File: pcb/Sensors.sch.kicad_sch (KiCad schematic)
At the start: 22 parts, among them J1 53398-0371, J2 53398-0371, J3 Conn_01x04_Pin, J4 53398-0371, J5 53398-0371, J6 53398-0371, J7 53398-0371, J8 53398-0371, J9 53398-0371, U2 BMP280

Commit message: Drobne poprawki w schemacie elektrycznym
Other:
- moved on the sheet: J3
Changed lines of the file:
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@@
 	(wire
 		(pts
-			(xy 198.12 72.39) (xy 198.12 69.85)
+			(xy 121.92 85.09) (xy 121.92 100.33)
 		)
 		(stroke
@@
 	(wire
 		(pts
-			(xy 121.92 85.09) (xy 121.92 100.33)
+			(xy 106.68 116.84) (xy 106.68 118.11)
 		)
 		(stroke
@@
 	(wire
 		(pts
-			(xy 106.68 116.84) (xy 106.68 118.11)
+			(xy 86.36 171.45) (xy 91.44 171.45)
 		)
 		(stroke
@@
 	(wire
 		(pts
-			(xy 86.36 171.45) (xy 91.44 171.45)
+			(xy 86.36 173.99) (xy 91.44 173.99)
 		)
 		(stroke
@@
 	(wire
 		(pts
-			(xy 86.36 173.99) (xy 91.44 173.99)
+			(xy 167.64 124.46) (xy 167.64 125.73)
 		)
 		(stroke
@@
 	(wire
 		(pts
-			(xy 167.64 124.46) (xy 167.64 125.73)
+			(xy 105.41 45.72) (xy 102.87 45.72)
 		)
 		(stroke
@@
 	(wire
 		(pts
-			(xy 105.41 45.72) (xy 102.87 45.72)
+			(xy 109.22 116.84) (xy 121.92 116.84)
 		)
 		(stroke
@@
 	(wire
 		(pts
-			(xy 109.22 116.84) (xy 121.92 116.84)
+			(xy 176.53 58.42) (xy 176.53 62.23)
 		)
 		(stroke
@@
 	(wire
 		(pts
+			(xy 176.53 67.31) (xy 180.34 67.31)
+		)
+		(stroke
+			(width 0)
+			(type default)
+		)
+	)
+	(wire
+		(pts
 			(xy 104.14 118.11) (xy 104.14 116.84)
 		)
@@
 	(wire
 		(pts
-			(xy 185.42 81.28) (xy 189.23 81.28)
-		)
-		(stroke
-			(width 0)
-			(type default)
-		)
-	)
-	(wire
-		(pts
 			(xy 121.92 50.8) (xy 123.19 50.8)
 		)
@@
 	(wire
 		(pts
-			(xy 198.12 69.85) (xy 185.42 69.85)
-		)
-		(stroke
-			(width 0)
-			(type default)
-		)
-	)
-	(wire
-		(pts
 			(xy 76.2 102.87) (xy 77.47 102.87)
 		)
@@
 	(wire
 		(pts
-			(xy 185.42 72.39) (xy 185.42 81.28)
-		)
-		(stroke
-			(width 0)
-			(type default)
-		)
-	)
-	(wire
-		(pts
 			(xy 78.74 106.68) (xy 77.47 106.68)
 		)
@@
 	(wire
 		(pts
-			(xy 185.42 64.77) (xy 189.23 64.77)
-		)
-		(stroke
-			(width 0)
-			(type default)
-		)
-	)
-	(wire
-		(pts
 			(xy 104.14 184.15) (xy 104.14 186.69)
 		)
@@
 	(wire
 		(pts
-			(xy 185.42 67.31) (xy 189.23 67.31)
+			(xy 123.19 48.26) (xy 123.19 50.8)
 		)
 		(stroke
@@
 	(wire
 		(pts
-			(xy 123.19 48.26) (xy 123.19 50.8)
+			(xy 176.53 69.85) (xy 180.34 69.85)
 		)
 		(stroke
@@
 	(wire
 		(pts
+			(xy 176.53 64.77) (xy 199.39 64.77)
+		)
+		(stroke
+			(width 0)
+			(type default)
+		)
+	)
+	(wire
+		(pts
 			(xy 73.66 160.02) (xy 73.66 179.07)
 		)
@@
 	(hierarchical_label "MQ135_AOUT"
 		(shape output)
-		(at 189.23 67.31 0)
+		(at 180.34 67.31 0)
 		(fields_autoplaced yes)
 		(effects
@@
 	(hierarchical_label "MQ135_DOUT"
 		(shape output)
-		(at 189.23 64.77 0)
+		(at 180.34 69.85 0)
 		(fields_autoplaced yes)
 		(effects
@@
 	(symbol
 		(lib_id "power:+3.3V")
-		(at 189.23 81.28 0)
+		(at 176.53 58.42 0)
 		(unit 1)
 		(exclude_from_sim no)
@@
 		(dnp no)
 		(property "Reference" "#PWR021"
-			(at 189.23 85.09 0)
+			(at 176.53 62.23 0)
 			(effects
 				(font
@@
 		)
 		(property "Value" "+3.3V"
-			(at 189.23 77.47 0)
+			(at 176.53 54.61 0)
 			(effects
 				(font
@@
 		)
 		(property "Footprint" ""
-			(at 189.23 81.28 0)
+			(at 176.53 58.42 0)
 			(effects
 				(font
@@
 		)
 		(property "Datasheet" ""
-			(at 189.23 81.28 0)
+			(at 176.53 58.42 0)
 			(effects
 				(font
@@
 		)
 		(property "Description" "Power symbol creates a global label with name \"+3.3V\""
-			(at 189.23 81.28 0)
+			(at 176.53 58.42 0)
 			(effects
 				(font
@@
 	(symbol
 		(lib_id "Connector:Conn_01x04_Pin")
-		(at 180.34 67.31 0)
+		(at 171.45 67.31 0)
+		(mirror x)
 		(unit 1)
 		(exclude_from_sim no)
@@
 		(on_board yes)
 		(dnp no)
-		(fields_autoplaced yes)
 		(property "Reference" "J3"
-			(at 180.975 59.69 0)
+			(at 172.085 74.93 0)
 			(effects
 				(font
@@
 		)
 		(property "Value" "Conn_01x04_Pin"
-			(at 180.975 62.23 0)
+			(at 172.085 72.39 0)
 			(effects
 				(font
@@
 		)
 		(property "Footprint" "1bmoje:533980471- MOLEXx4"
-			(at 180.34 67.31 0)
+			(at 171.45 67.31 0)
 			(effects
 				(font
@@
 		)
 		(property "Datasheet" "~"
-			(at 180.34 67.31 0)
+			(at 171.45 67.31 0)
 			(effects
 				(font
@@
 		)
 		(property "Description" "Generic connector, single row, 01x04, script generated"
-			(at 180.34 67.31 0)
+			(at 171.45 67.31 0)
 			(effects
 				(font
@@
 	(symbol
 		(lib_id "power:GND")
-		(at 198.12 72.39 0)
+		(at 199.39 64.77 0)
 		(unit 1)
 		(exclude_from_sim no)
@@
 		(fields_autoplaced yes)
 		(property "Reference" "#PWR022"
-			(at 198.12 78.74 0)
+			(at 199.39 71.12 0)
 			(effects
 				(font
@@
 		)
 		(property "Value" "GND"
-			(at 198.12 77.47 0)
+			(at 199.39 69.85 0)
 			(effects
 				(font
@@
 		)
 		(property "Footprint" ""
-			(at 198.12 72.39 0)
+			(at 199.39 64.77 0)
 			(effects
 				(font
@@
 		)
 		(property "Datasheet" ""
-			(at 198.12 72.39 0)
+			(at 199.39 64.77 0)
 			(effects
 				(font
@@
 		)
 		(property "Description" "Power symbol creates a global label with name \"GND\" , ground"
-			(at 198.12 72.39 0)
+			(at 199.39 64.77 0)
 			(effects
 				(font

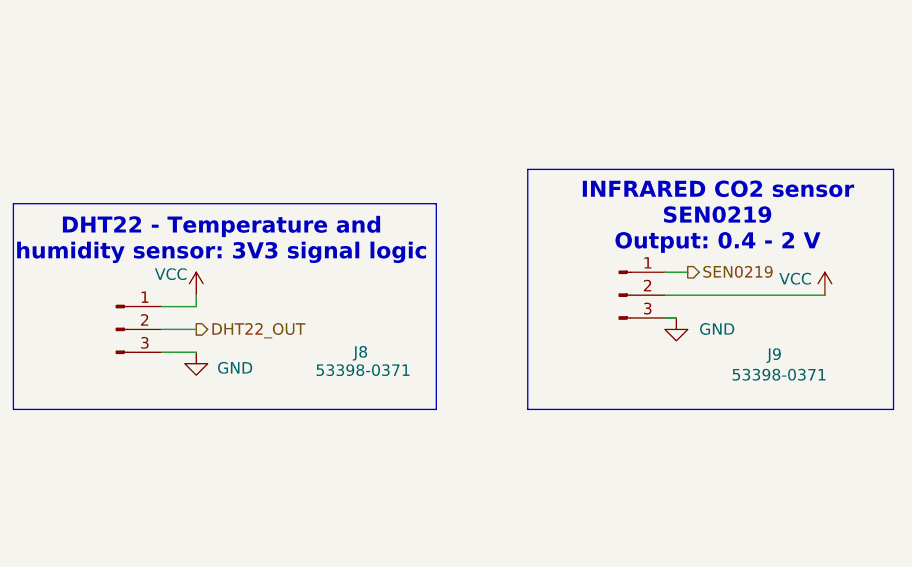
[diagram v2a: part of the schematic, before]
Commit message: PCB jeszcze mniejsza wersja
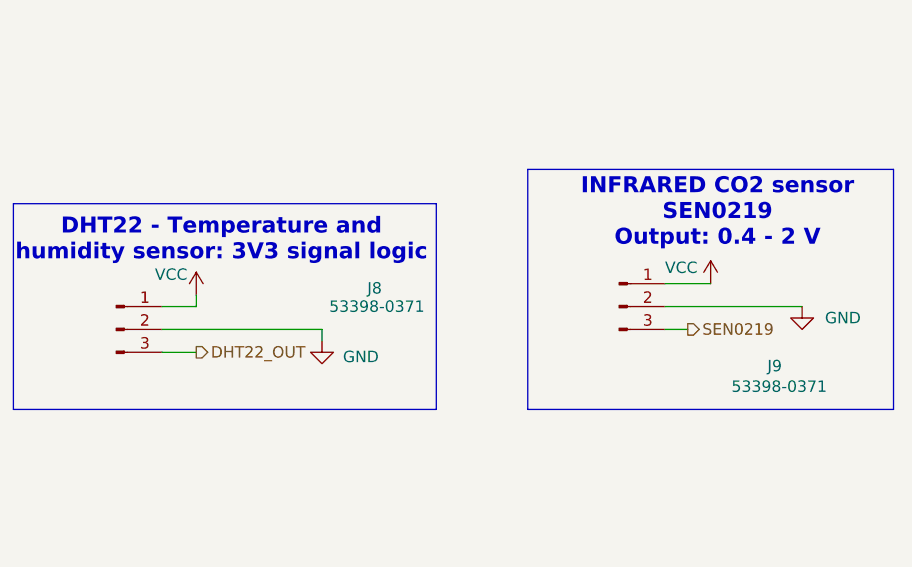
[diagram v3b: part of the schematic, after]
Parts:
- J1: footprint 53398-0371 -> Connector_PinHeader_2.54mm:PinHeader_1x03_P2.54mm_Vertical
- J2, J4, J5, J6, J7, J8, J9: footprint 1bmoje:53398-0371 -> Connector_PinHeader_2.54mm:PinHeader_1x03_P2.54mm_Vertical
- J3: footprint 1bmoje:533980471- MOLEXx4 -> Connector_PinHeader_2.54mm:PinHeader_1x04_P2.54mm_Vertical
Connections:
- net DHT22_OUT: now also J8.3 (Pin_3); no longer J8.2 (Pin_2)
- net GND: now also J8.2 (Pin_2), J9.2 (Pin_2); no longer J8.3 (Pin_3), J9.3 (Pin_3)
- net SEN0219: now also J9.3 (Pin_3); no longer J9.1 (Pin_1)
- net VCC: now also J9.1 (Pin_1); no longer J9.2 (Pin_2)
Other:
- moved on the sheet: J9

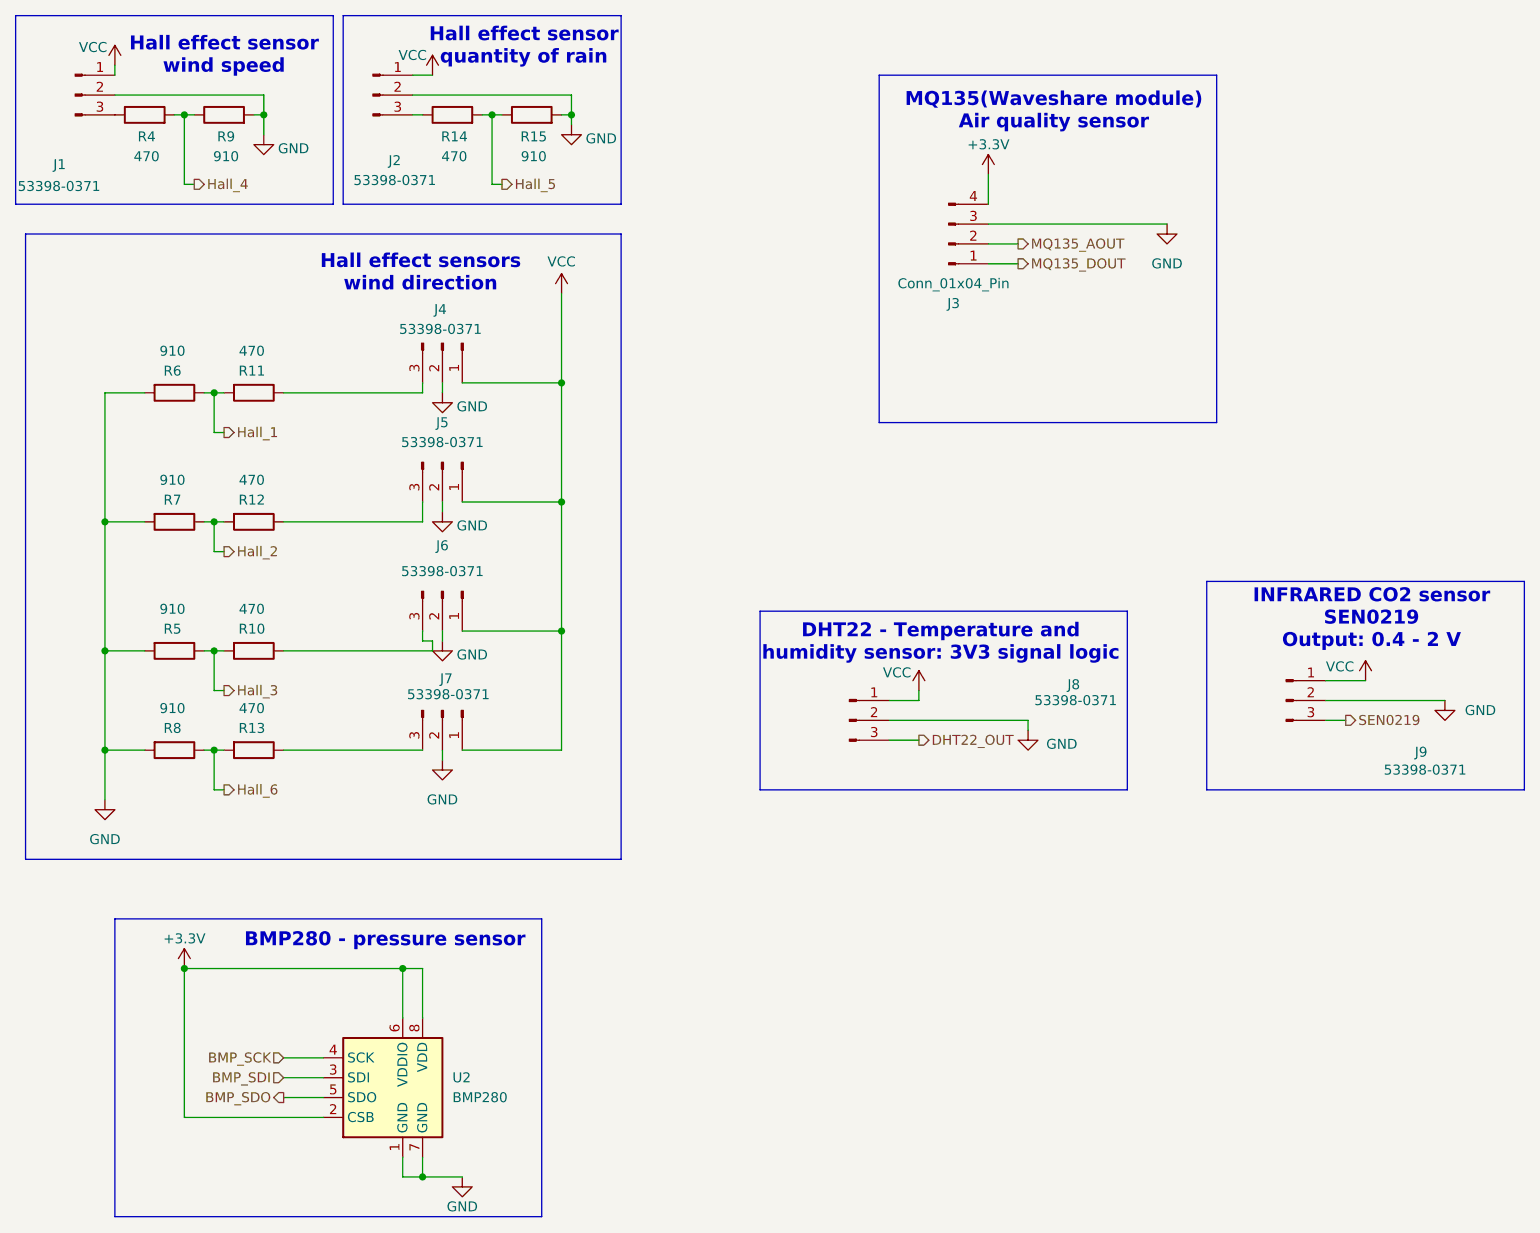
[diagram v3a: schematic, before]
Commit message: 4 layer PCB
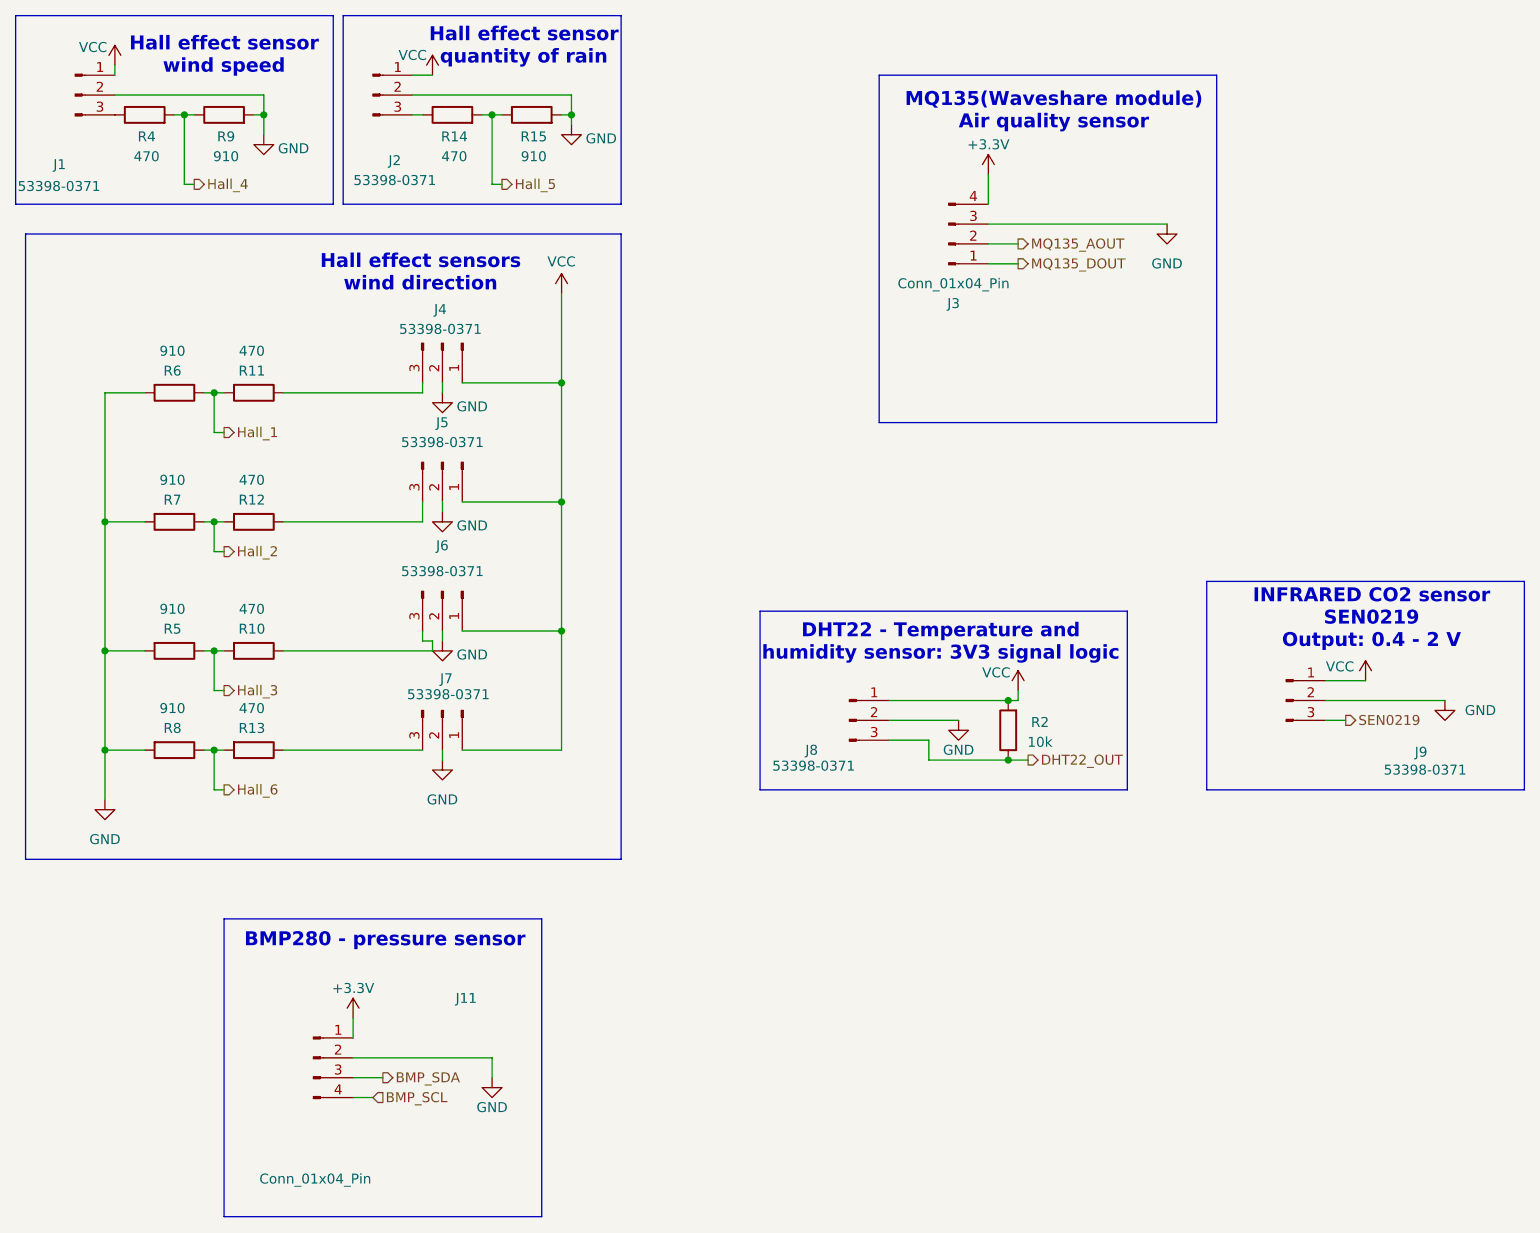
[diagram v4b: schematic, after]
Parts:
- removed U2: BMP280, Package_LGA:Bosch_LGA-8_2x2.5mm_P0.65mm_ClockwisePinNumbering, symbol Sensor_Pressure:BMP280
- added J11: Conn_01x04_Pin, Connector_PinHeader_2.54mm:PinHeader_1x04_P2.54mm_Vertical, symbol Connector:Conn_01x04_Pin
- added R2: 10k, Resistor_SMD:R_0603_1608Metric, symbol Device:R
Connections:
- net +3.3V: now also J11.1 (Pin_1)
- net DHT22_OUT: now also R2.1
- net GND: now also J11.2 (Pin_2)
- net VCC: now also R2.2
- new net BMP_SCL: J11.4 (Pin_4)
- new net BMP_SDA: J11.3 (Pin_3)
